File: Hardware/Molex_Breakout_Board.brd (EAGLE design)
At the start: 34.3 x 33.7 mm, 22 parts

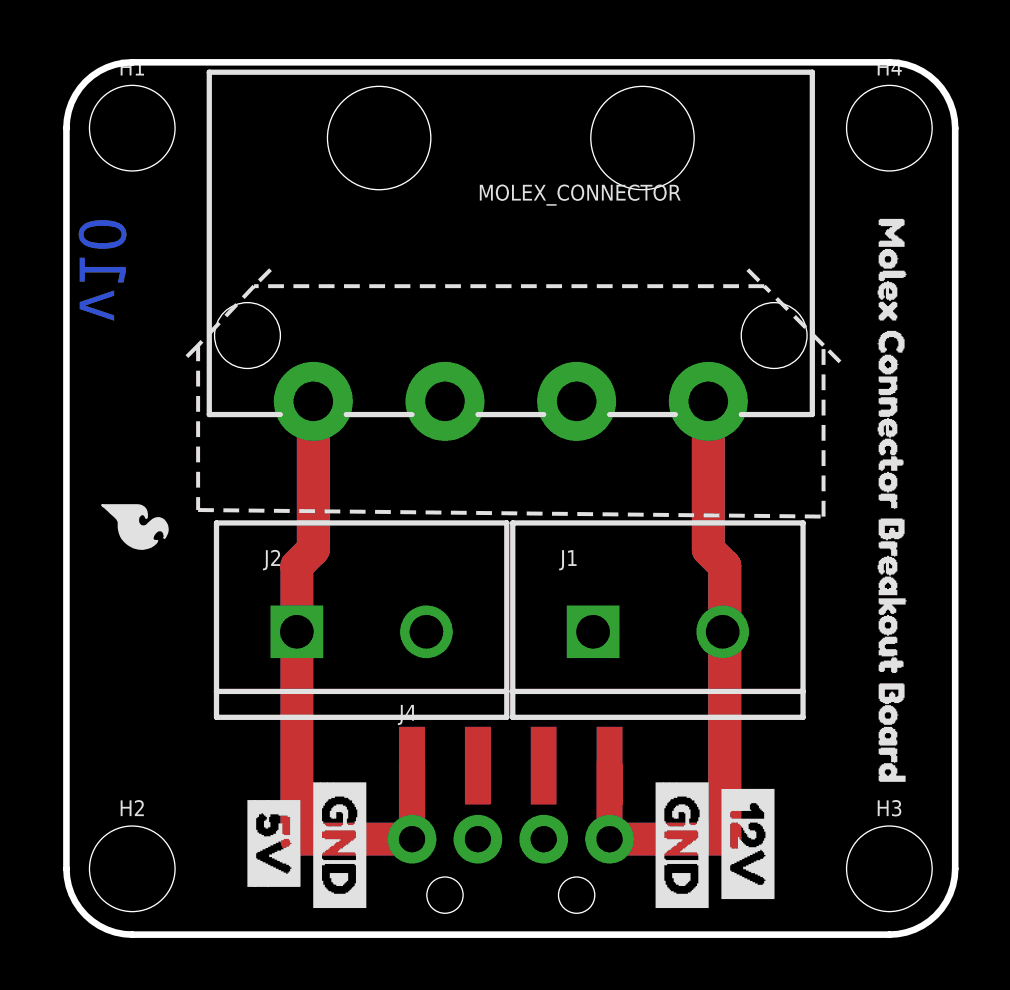
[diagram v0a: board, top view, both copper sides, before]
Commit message: Shorten Length of Voltage Rails
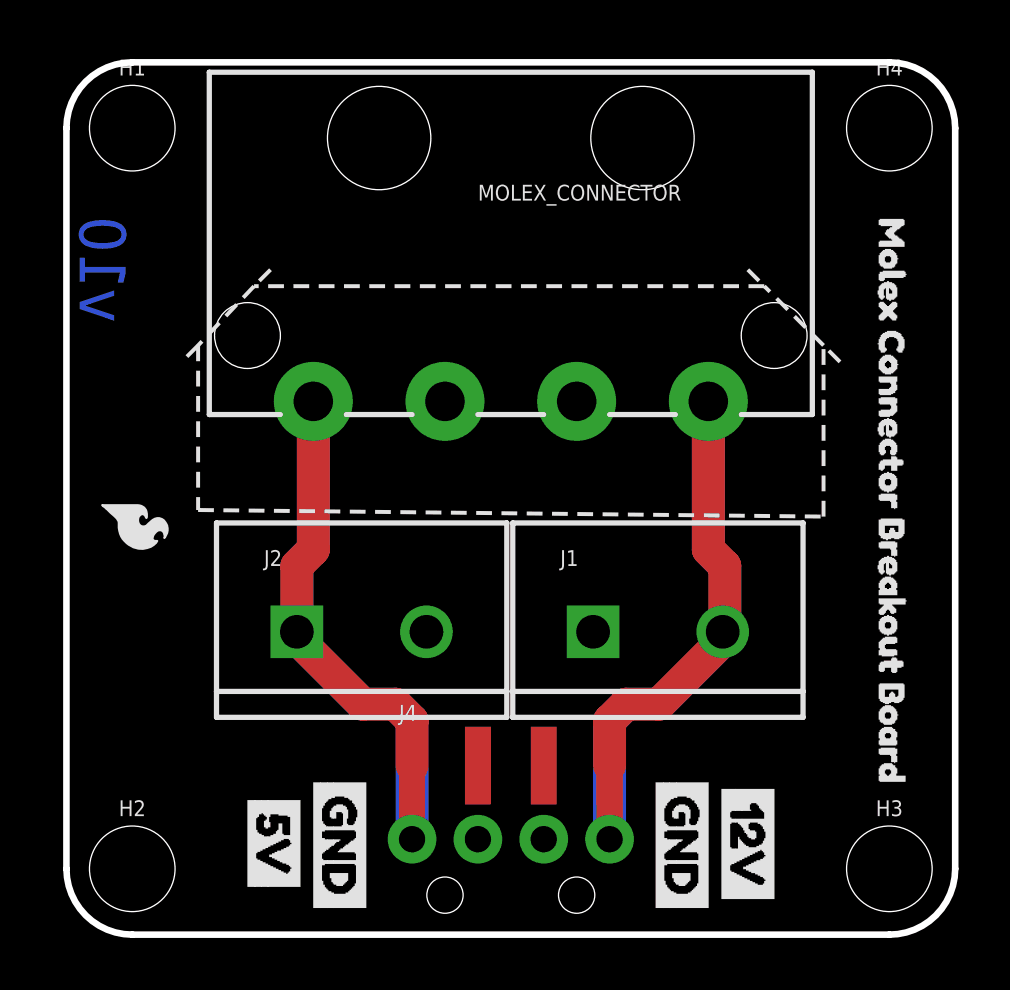
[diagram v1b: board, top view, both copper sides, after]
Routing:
- net 5V: track 46.0 -> 39.2 mm
- net 12V: track 46.2 -> 39.9 mm
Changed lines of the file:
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@@
 <wire x1="9.525" y1="14.859" x2="8.89" y2="14.224" width="1.27" layer="1"/>
 <wire x1="8.89" y1="14.224" x2="8.89" y2="11.684" width="1.27" layer="1"/>
-<wire x1="8.89" y1="3.683" x2="13.335" y2="3.683" width="1.27" layer="1"/>
-<wire x1="8.89" y1="11.684" x2="8.89" y2="3.683" width="1.27" layer="1"/>
-<wire x1="8.89" y1="3.683" x2="13.335" y2="3.683" width="1.27" layer="16"/>
-<wire x1="8.89" y1="11.684" x2="8.89" y2="3.683" width="1.27" layer="16"/>
+<wire x1="13.335" y1="6.524" x2="13.335" y2="8.255" width="1.27" layer="1"/>
+<wire x1="13.335" y1="8.255" x2="12.7" y2="8.89" width="1.27" layer="1"/>
+<wire x1="12.7" y1="8.89" x2="11.43" y2="8.89" width="1.27" layer="1"/>
+<wire x1="11.43" y1="8.89" x2="8.89" y2="11.43" width="1.27" layer="1"/>
+<wire x1="8.89" y1="11.43" x2="8.89" y2="11.684" width="1.27" layer="1"/>
+<wire x1="8.89" y1="11.43" x2="11.43" y2="8.89" width="1.27" layer="16"/>
+<wire x1="11.43" y1="8.89" x2="12.7" y2="8.89" width="1.27" layer="16"/>
+<wire x1="12.7" y1="8.89" x2="13.335" y2="8.255" width="1.27" layer="16"/>
+<wire x1="13.335" y1="8.255" x2="13.335" y2="3.683" width="1.27" layer="16"/>
 </signal>
 <signal name="12V">
 <wire x1="24.765" y1="20.701" x2="24.765" y2="14.859" width="1.27" layer="1"/>
-<wire x1="24.765" y1="14.859" x2="25.4" y2="14.224" width="1.27" layer="1"/>
+<wire x1="25.4" y1="14.224" x2="24.765" y2="14.859" width="1.27" layer="1"/>
 <contactref element="MOLEX_CONNECTOR" pad="12V"/>
 <contactref element="J1" pad="2"/>
@@
 <wire x1="24.765" y1="20.574" x2="24.765" y2="14.859" width="1.27" layer="16"/>
 <wire x1="24.765" y1="14.859" x2="25.4" y2="14.224" width="1.27" layer="16"/>
-<wire x1="20.955" y1="3.683" x2="25.4" y2="3.683" width="1.27" layer="16"/>
-<wire x1="25.4" y1="3.683" x2="20.955" y2="3.683" width="1.27" layer="1"/>
-<wire x1="25.4" y1="14.224" x2="25.4" y2="3.683" width="1.27" layer="1"/>
-<wire x1="25.4" y1="3.683" x2="25.4" y2="11.684" width="1.27" layer="16"/>
-<wire x1="25.4" y1="11.684" x2="25.32" y2="11.684" width="1.27" layer="16"/>
-<wire x1="25.4" y1="14.224" x2="25.4" y2="11.684" width="1.27" layer="16"/>
+<wire x1="20.955" y1="6.524" x2="20.955" y2="8.255" width="1.27" layer="1"/>
+<wire x1="20.955" y1="8.255" x2="21.59" y2="8.89" width="1.27" layer="1"/>
+<wire x1="22.86" y1="8.89" x2="21.59" y2="8.89" width="1.27" layer="1"/>
+<wire x1="25.4" y1="11.43" x2="22.86" y2="8.89" width="1.27" layer="1"/>
+<wire x1="25.4" y1="11.43" x2="22.86" y2="8.89" width="1.27" layer="16"/>
+<wire x1="21.59" y1="8.89" x2="22.86" y2="8.89" width="1.27" layer="16"/>
+<wire x1="21.59" y1="8.89" x2="20.955" y2="8.255" width="1.27" layer="16"/>
+<wire x1="20.955" y1="8.255" x2="20.955" y2="3.683" width="1.27" layer="16"/>
+<wire x1="25.4" y1="11.43" x2="25.4" y2="14.224" width="1.27" layer="1"/>
+<wire x1="25.4" y1="14.224" x2="25.4" y2="11.43" width="1.27" layer="16"/>
+<wire x1="25.32" y1="11.684" x2="25.4" y2="11.604" width="0.254" layer="1"/>
+<wire x1="25.4" y1="11.604" x2="25.4" y2="11.43" width="0.254" layer="1"/>
 </signal>
 </signals>

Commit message: Update Molex_Breakout_Board.brd
- Update Molex through holes for straight connector
- adjust 5mm screw terminal spacing when slide-locking them together
- reroute traces based on adjustments
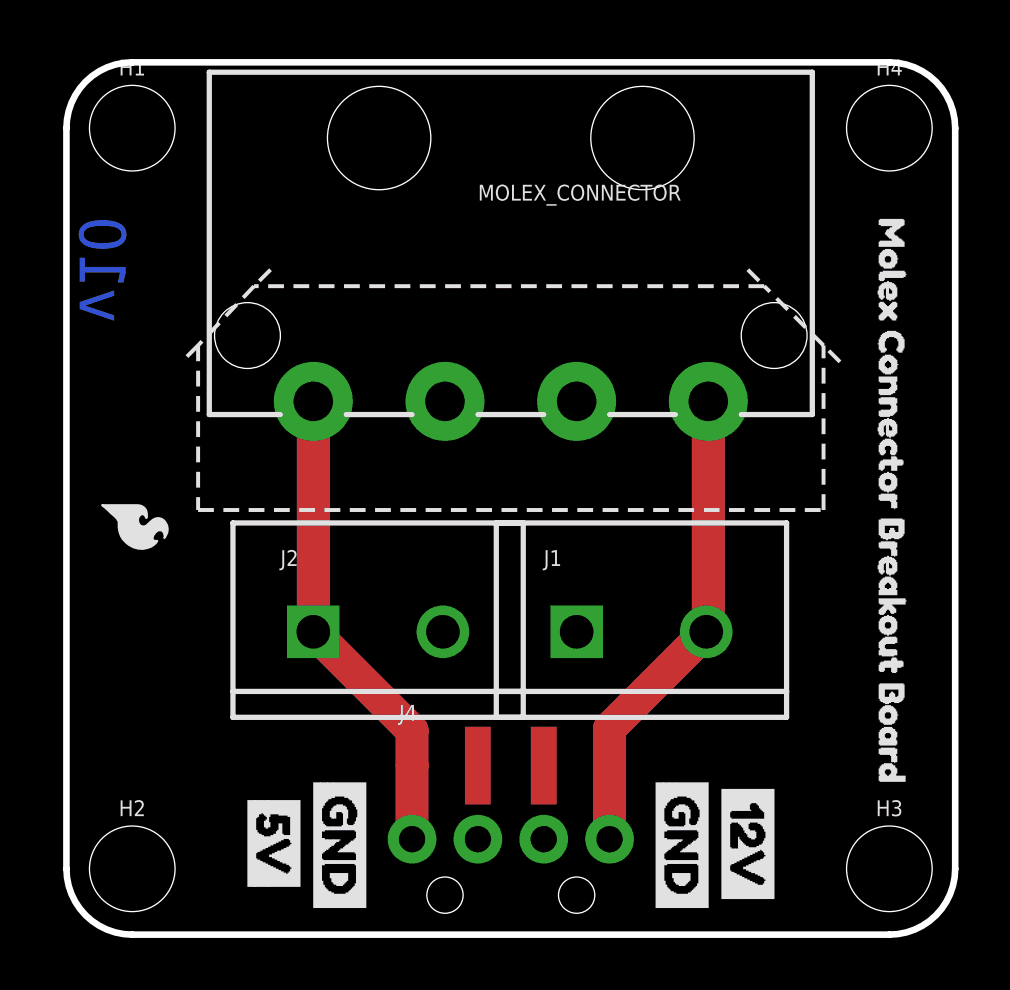
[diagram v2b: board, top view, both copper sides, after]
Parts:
- moved J1 0.64 mm to (19.7, 11.7)
- moved J2 0.63 mm to (9.53, 11.7)
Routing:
- net 12V: track 39.9 -> 37.0 mm
- net 5V: track 39.2 -> 37.1 mm
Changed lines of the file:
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@@
 <wire x1="31.75" y1="33.655" x2="34.29" y2="31.115" width="0.254" layer="20" curve="-90"/>
 <wire x1="5.08" y1="22.733" x2="5.08" y2="16.383" width="0.1524" layer="21" style="shortdash"/>
-<wire x1="5.08" y1="16.383" x2="29.21" y2="16.129" width="0.1524" layer="21" style="shortdash"/>
-<wire x1="29.21" y1="16.129" x2="29.21" y2="22.733" width="0.1524" layer="21" style="shortdash"/>
+<wire x1="5.08" y1="16.383" x2="29.21" y2="16.383" width="0.1524" layer="21" style="shortdash"/>
+<wire x1="29.21" y1="16.383" x2="29.21" y2="22.733" width="0.1524" layer="21" style="shortdash"/>
 <wire x1="29.21" y1="22.733" x2="26.924" y2="25.019" width="0.1524" layer="21" style="shortdash"/>
 <wire x1="26.924" y1="25.019" x2="7.239" y2="25.019" width="0.1524" layer="21" style="shortdash"/>
@@
 <element name="LOGO1" library="SparkFun-Aesthetics" package="OSHW-LOGO-S" value="OSHW-LOGOS" x="17.145" y="29.464" rot="MR0"/>
 <element name="LOGO2" library="SparkFun-Aesthetics" package="SFE_LOGO_NAME_FLAME_.1" value="SFE_LOGO_NAME_FLAME.1_INCH" x="23.495" y="21.844" rot="MR0"/>
-<element name="J1" library="SparkFun-Connectors" package="SCREWTERMINAL-5MM-2" value="" x="20.32" y="11.684">
-<attribute name="SF_SKU" value="PRT-08432" x="20.32" y="11.684" size="1.778" layer="27" font="vector" ratio="15" display="off"/>
-</element>
-<element name="J2" library="SparkFun-Connectors" package="SCREWTERMINAL-5MM-2" value="" x="8.89" y="11.684">
-<attribute name="SF_SKU" value="PRT-08432" x="8.89" y="11.684" size="1.778" layer="27" font="vector" ratio="15" display="off"/>
+<element name="J1" library="SparkFun-Connectors" package="SCREWTERMINAL-5MM-2" value="" x="19.685" y="11.684">
+<attribute name="SF_SKU" value="PRT-08432" x="19.685" y="11.684" size="1.778" layer="27" font="vector" ratio="15" display="off"/>
+</element>
+<element name="J2" library="SparkFun-Connectors" package="SCREWTERMINAL-5MM-2" value="" x="9.525" y="11.684">
+<attribute name="SF_SKU" value="PRT-08432" x="9.525" y="11.684" size="1.778" layer="27" font="vector" ratio="15" display="off"/>
 </element>
 <element name="J3" library="SparkFun-Connectors" package="1X04" value="" x="13.335" y="3.683" rot="MR180">
@@
 <contactref element="J2" pad="1"/>
 <contactref element="J3" pad="1"/>
-<wire x1="8.89" y1="14.224" x2="8.89" y2="11.684" width="1.27" layer="16"/>
-<wire x1="9.525" y1="20.574" x2="9.525" y2="14.859" width="1.27" layer="16"/>
-<wire x1="9.525" y1="14.859" x2="8.89" y2="14.224" width="1.27" layer="16"/>
 <contactref element="J4" pad="1"/>
-<wire x1="13.335" y1="6.524" x2="13.335" y2="3.683" width="1.016" layer="1"/>
-<wire x1="9.525" y1="20.574" x2="9.525" y2="14.859" width="1.27" layer="1"/>
-<wire x1="9.525" y1="14.859" x2="8.89" y2="14.224" width="1.27" layer="1"/>
-<wire x1="8.89" y1="14.224" x2="8.89" y2="11.684" width="1.27" layer="1"/>
-<wire x1="13.335" y1="6.524" x2="13.335" y2="8.255" width="1.27" layer="1"/>
-<wire x1="13.335" y1="8.255" x2="12.7" y2="8.89" width="1.27" layer="1"/>
-<wire x1="12.7" y1="8.89" x2="11.43" y2="8.89" width="1.27" layer="1"/>
-<wire x1="11.43" y1="8.89" x2="8.89" y2="11.43" width="1.27" layer="1"/>
-<wire x1="8.89" y1="11.43" x2="8.89" y2="11.684" width="1.27" layer="1"/>
-<wire x1="8.89" y1="11.43" x2="11.43" y2="8.89" width="1.27" layer="16"/>
-<wire x1="11.43" y1="8.89" x2="12.7" y2="8.89" width="1.27" layer="16"/>
-<wire x1="12.7" y1="8.89" x2="13.335" y2="8.255" width="1.27" layer="16"/>
-<wire x1="13.335" y1="8.255" x2="13.335" y2="3.683" width="1.27" layer="16"/>
+<wire x1="9.525" y1="20.574" x2="9.525" y2="11.684" width="1.27" layer="1"/>
+<wire x1="13.335" y1="3.683" x2="13.335" y2="7.874" width="1.27" layer="16"/>
+<wire x1="13.335" y1="7.874" x2="9.525" y2="11.684" width="1.27" layer="16"/>
+<wire x1="13.335" y1="7.874" x2="9.525" y2="11.684" width="1.27" layer="1"/>
+<wire x1="13.335" y1="3.683" x2="13.335" y2="6.524" width="1.27" layer="1"/>
+<wire x1="13.335" y1="6.524" x2="13.335" y2="7.874" width="1.27" layer="1"/>
+<wire x1="9.525" y1="20.701" x2="9.525" y2="11.684" width="1.27" layer="16"/>
 </signal>
 <signal name="12V">
-<wire x1="24.765" y1="20.701" x2="24.765" y2="14.859" width="1.27" layer="1"/>
-<wire x1="25.4" y1="14.224" x2="24.765" y2="14.859" width="1.27" layer="1"/>
 <contactref element="MOLEX_CONNECTOR" pad="12V"/>
 <contactref element="J1" pad="2"/>
 <contactref element="J3" pad="4"/>
 <contactref element="J4" pad="4"/>
-<wire x1="20.955" y1="6.524" x2="20.955" y2="3.683" width="1.016" layer="1"/>
-<wire x1="24.765" y1="20.574" x2="24.765" y2="14.859" width="1.27" layer="16"/>
-<wire x1="24.765" y1="14.859" x2="25.4" y2="14.224" width="1.27" layer="16"/>
-<wire x1="20.955" y1="6.524" x2="20.955" y2="8.255" width="1.27" layer="1"/>
-<wire x1="20.955" y1="8.255" x2="21.59" y2="8.89" width="1.27" layer="1"/>
-<wire x1="22.86" y1="8.89" x2="21.59" y2="8.89" width="1.27" layer="1"/>
-<wire x1="25.4" y1="11.43" x2="22.86" y2="8.89" width="1.27" layer="1"/>
-<wire x1="25.4" y1="11.43" x2="22.86" y2="8.89" width="1.27" layer="16"/>
-<wire x1="21.59" y1="8.89" x2="22.86" y2="8.89" width="1.27" layer="16"/>
-<wire x1="21.59" y1="8.89" x2="20.955" y2="8.255" width="1.27" layer="16"/>
-<wire x1="20.955" y1="8.255" x2="20.955" y2="3.683" width="1.27" layer="16"/>
-<wire x1="25.4" y1="11.43" x2="25.4" y2="14.224" width="1.27" layer="1"/>
-<wire x1="25.4" y1="14.224" x2="25.4" y2="11.43" width="1.27" layer="16"/>
-<wire x1="25.32" y1="11.684" x2="25.4" y2="11.604" width="0.254" layer="1"/>
-<wire x1="25.4" y1="11.604" x2="25.4" y2="11.43" width="0.254" layer="1"/>
+<wire x1="24.765" y1="20.574" x2="24.765" y2="11.764" width="1.27" layer="1"/>
+<wire x1="24.765" y1="11.764" x2="24.685" y2="11.684" width="1.27" layer="1"/>
+<wire x1="20.955" y1="3.683" x2="20.955" y2="7.954" width="1.27" layer="16"/>
+<wire x1="20.955" y1="7.954" x2="24.685" y2="11.684" width="1.27" layer="16"/>
+<wire x1="20.955" y1="3.683" x2="20.955" y2="6.524" width="1.27" layer="1"/>
+<wire x1="20.955" y1="7.954" x2="24.685" y2="11.684" width="1.27" layer="1"/>
+<wire x1="20.955" y1="6.524" x2="20.955" y2="7.954" width="1.27" layer="1"/>
+<wire x1="24.765" y1="20.574" x2="24.765" y2="11.811" width="1.27" layer="16"/>
+<wire x1="24.765" y1="11.811" x2="24.638" y2="11.684" width="1.27" layer="16"/>
 </signal>
 </signals>
